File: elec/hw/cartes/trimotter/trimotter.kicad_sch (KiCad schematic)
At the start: 68 parts, among them J2 22053051, J3 2-1445055-2, J4 2-1445055-3, J5 3-794630-6, J6 3-794630-4, Q1 2N7002, U1 DRV8243HQDGQRQ1, U2 SN74LVC2T45DCU, U4 PCA9535PW

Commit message: trimotter schematic corrected after review. component placement done, routing tbd
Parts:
- removed R13: 10k 1%, cocotter_resistor:r0603_reflow, symbol cocotter_resistors:R_10k_0603_1%
- removed R14: 470R 1%, cocotter_resistor:r0603_reflow, symbol cocotter_resistors:R_470R_0603_1%
- added R13, R33, R34: 3k3 1%, cocotter_resistor:r0603_reflow, symbol cocotter_resistors:R_3k3_0603_1%
- added R14, R32: 1k 1%, cocotter_resistor:r0603_reflow, symbol cocotter_resistors:R_1k_0603_1%
- added R30, R31, R35: 0R, cocotter_resistor:r0603_reflow, symbol cocotter_resistors:R_0R_0603
- C3: value 1µF 50V -> 47µF 10V; footprint cocotter_capacitors:C_0805_2012Metric -> cocotter_capacitors:C_1206_3216Metric; symbol cocotter_capacitors:C_1µF_50V_0805 -> cocotter_capacitors:C_47µF_10V_1206_X5R; JLCPCB Part # C28323 -> C96123; Specification 1µF 50V X7R 0805 -> 47µF 10V X5R 1206
- D1, D3: value green, 0603 -> green, 1206; footprint cocotter_diodes:LED_0603_1608Metric -> cocotter_diodes:24-21-1206_reverse_mount; symbol cocotter_diodes:green_led_0603 -> cocotter_diodes:green_led_1206_reverse_mount; DIGIKEY_REF 3147-B19Y1UYG-20C000313U1930CT-ND -> (none); JLCPCB Part # C22371299 -> C2980185; MOUSER_REF 710-150060VS55040 -> (none)
- D2: value yellow, 0603 -> red, 1206; footprint cocotter_diodes:LED_0603_1608Metric -> cocotter_diodes:24-21-1206_reverse_mount; symbol cocotter_diodes:yellow_led_0603 -> cocotter_diodes:red_led_1206_reverse_mount; DIGIKEY_REF 150060YS55040 -> (none); JLCPCB Part # C965802 -> C2827254
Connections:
- net +3V3: now also R14.2, R32.2
- net VMOT: now also J4.2, R33.1
- net brake_3v3: now also U4.7 (IO0_3), R35.2; no longer J1.4 (brake_3v3), U4.5 (IO0_1)
- net ctc_left_3v3: now also U4.5 (IO0_1); no longer U4.7 (IO0_3)
- net ctc_right_3v3: now also U4.4 (IO0_0); no longer U4.6 (IO0_2)
- net encoder_A_5v: now also R30.2; no longer U2.6 (B2)
- net encoder_B_5v: now also R31.2; no longer U2.7 (B1)
- net nFAULT_3V3: now also U4.6 (IO0_2); no longer U4.4 (IO0_0)
- net vmot_absent_3v3: now also U4.20 (IO1_7); no longer U4.10 (IO0_6)
- net at TP5.1: now also U4.15 (IO1_2); no longer U4.16 (IO1_3)
- net at TP7.1: now also U4.17 (IO1_4); no longer U4.18 (IO1_5)
- net at D2.A: now also R14.1, R32.1
- net at D1.A: now also R13.2
- net at TP8.1: now also U4.18 (IO1_5); no longer U4.19 (IO1_6)
- net at TP9.1: now also U4.19 (IO1_6); no longer U4.20 (IO1_7)
- net at TP2.1: now also U4.10 (IO0_6); no longer U4.13 (IO1_0)
- net at TP3.1: now also U4.13 (IO1_0); no longer U4.14 (IO1_1)
- net at TP4.1: now also U4.14 (IO1_1); no longer U4.15 (IO1_2)
- net at TP6.1: now also U4.16 (IO1_3); no longer U4.17 (IO1_4)
- new net: J1.4 (brake_3v3), R35.1
- new net: R33.2, R34.1
- new net: R30.1, U2.6 (B2)
- new net: R31.1, U2.7 (B1)
- new net: R13.1, R34.2
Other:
- moved on the sheet: C3, D1, Q1, R27, R28, R29, TP2, TP3, TP4, TP5, TP6, TP7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

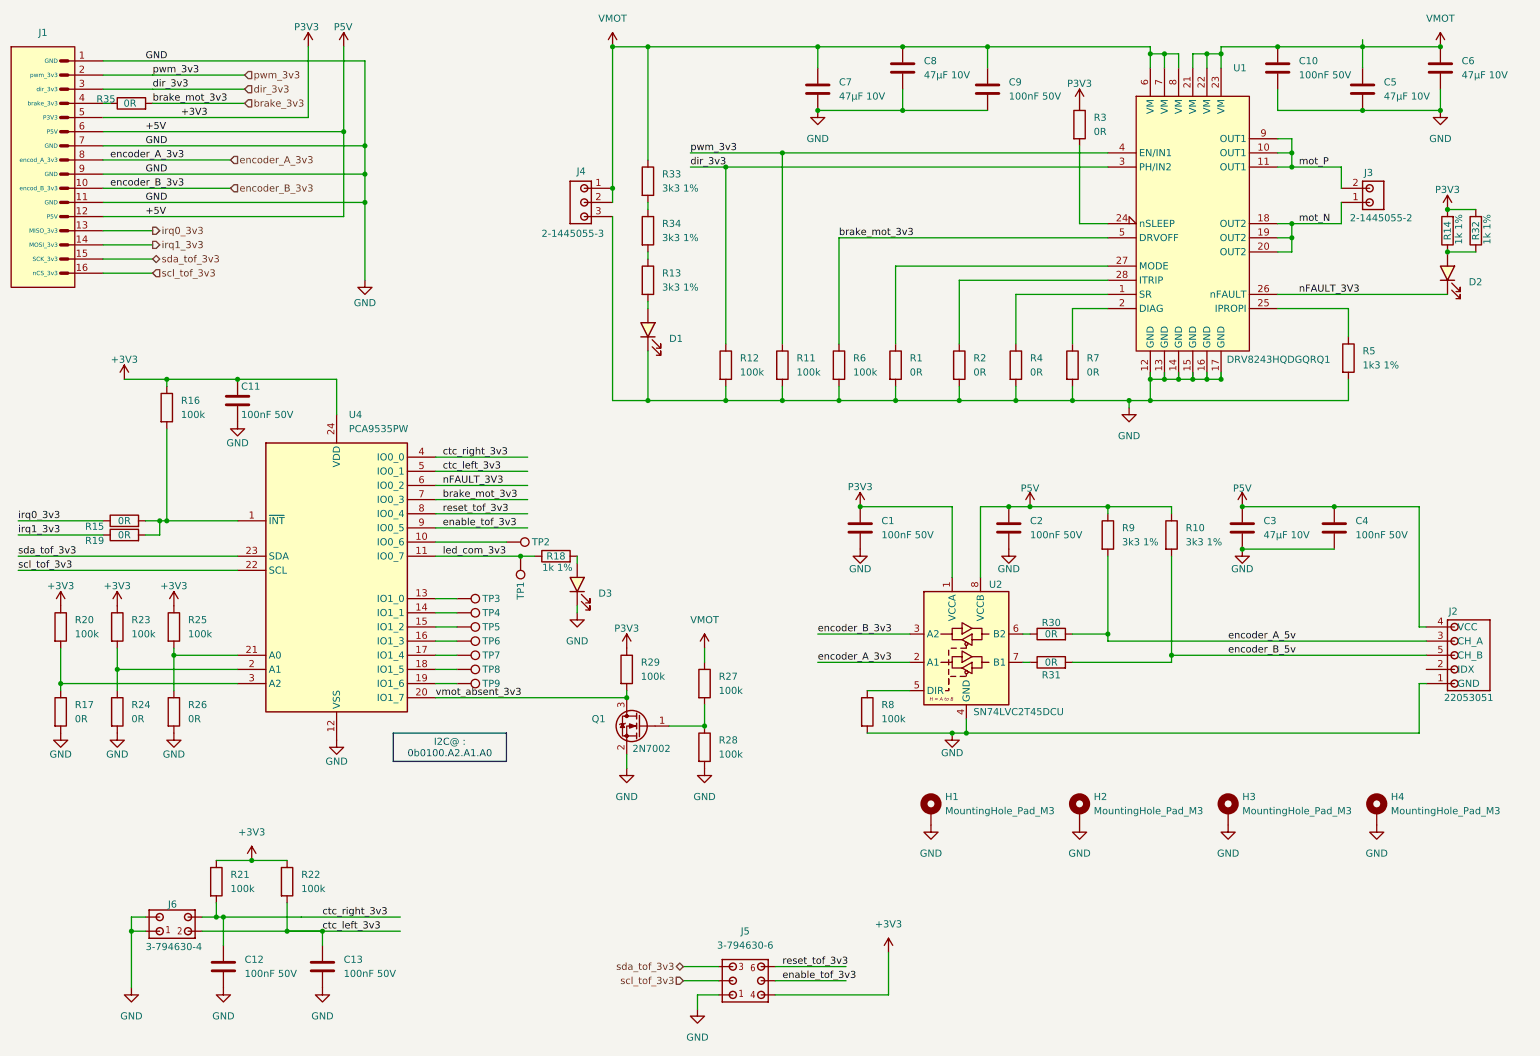
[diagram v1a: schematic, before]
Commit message: trimotter routing ready to review
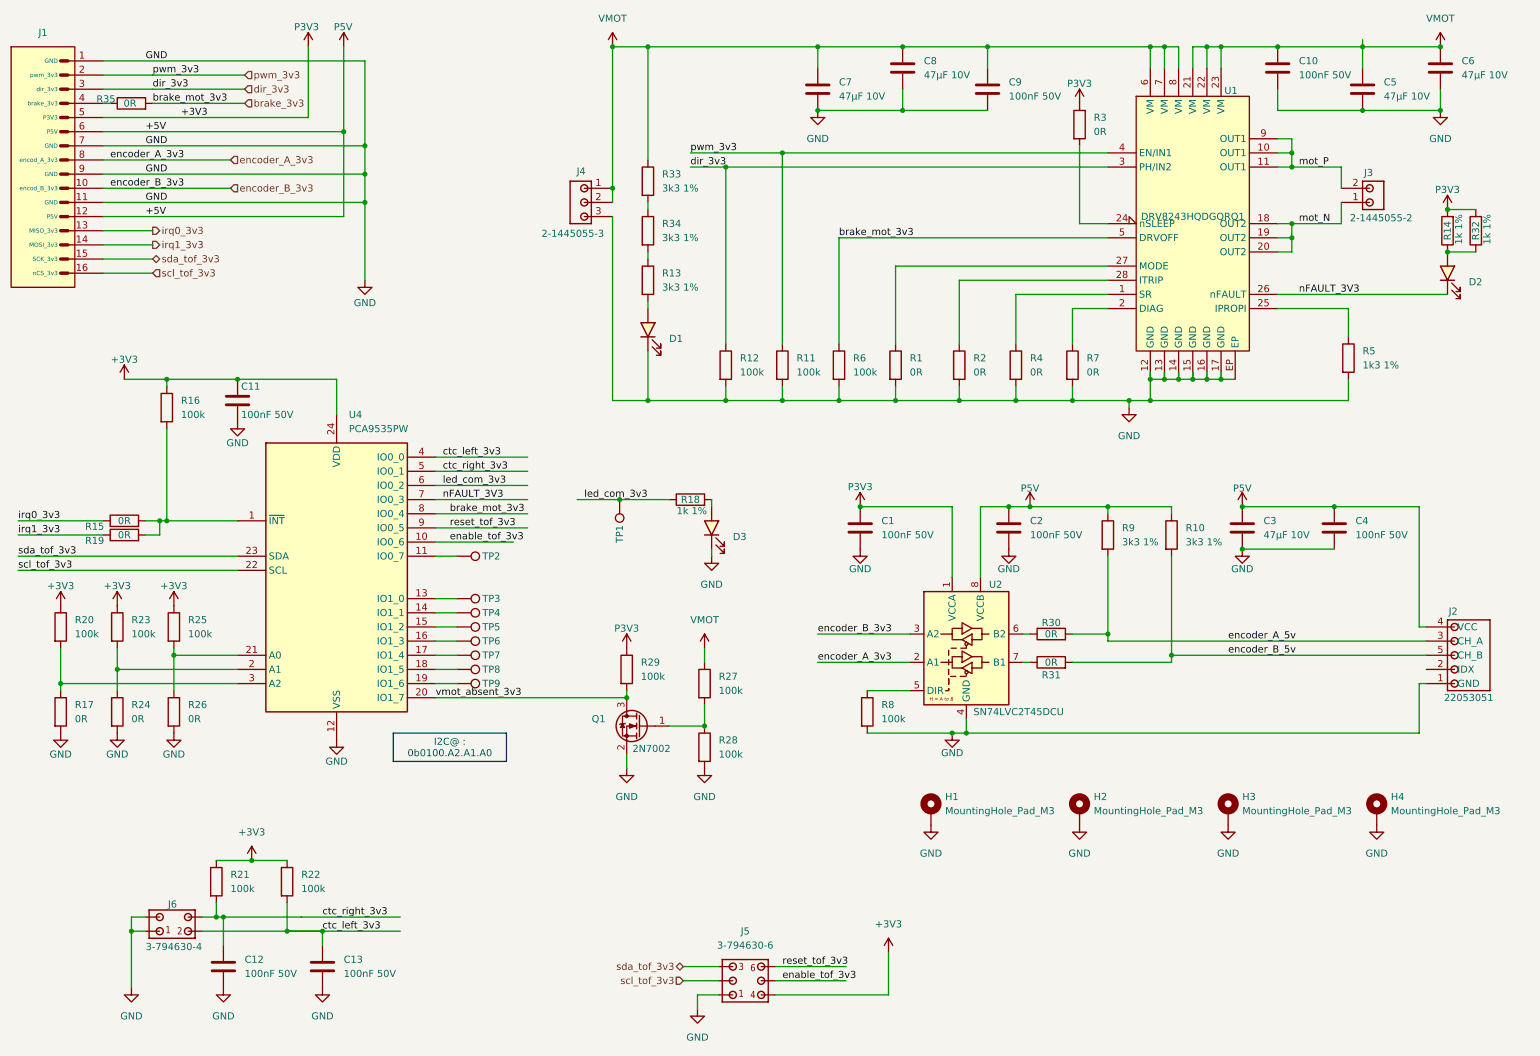
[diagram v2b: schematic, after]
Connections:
- net GND: now also U1.EP
- net brake_3v3: now also U4.8 (IO0_4); no longer U4.7 (IO0_3)
- net ctc_left_3v3: now also U4.4 (IO0_0); no longer U4.5 (IO0_1)
- net ctc_right_3v3: now also U4.5 (IO0_1); no longer U4.4 (IO0_0)
- net enable_tof_3v3: now also U4.10 (IO0_6); no longer U4.9 (IO0_5)
- net led_com_3v3: now also U4.6 (IO0_2); no longer U4.11 (IO0_7)
- net nFAULT_3V3: now also U4.7 (IO0_3); no longer U4.6 (IO0_2)
- net reset_tof_3v3: now also U4.9 (IO0_5); no longer U4.8 (IO0_4)
- net at TP2.1: now also U4.11 (IO0_7); no longer U4.10 (IO0_6)
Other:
- moved on the sheet: D3, R18

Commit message: jlcpcb part added
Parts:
- H1, H2, H3, H4: now in the parts list
- J1: JLCPCB Part # (none) -> C720217
- J2: JLCPCB Part # (none) -> C586992
- J3: JLCPCB Part # (none) -> C239446
- J4: JLCPCB Part # (none) -> C239447
- U1: JLCPCB Part # (none) -> C5250151
- U2: JLCPCB Part # (none) -> C15741
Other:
- moved on the sheet: R18, R5, TP1
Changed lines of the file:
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@@
 	)
 	(junction
-		(at 124.46 100.33)
-		(diameter 0)
-		(color 0 0 0 0)
-	)
-	(junction
 		(at 257.81 30.48)
 		(diameter 0)
@@
 	)
 	(junction
+		(at 124.46 97.79)
+		(diameter 0)
+		(color 0 0 0 0)
+	)
+	(junction
 		(at 44.45 128.27)
 		(diameter 0)
@@
 	(wire
 		(pts
-			(xy 116.84 100.33) (xy 124.46 100.33)
-		)
-		(stroke
-			(width 0)
-			(type default)
-		)
-	)
-	(wire
-		(pts
 			(xy 267.97 133.35) (xy 267.97 142.24)
 		)
@@
 	(wire
 		(pts
-			(xy 91.44 97.79) (xy 107.95 97.79)
+			(xy 91.44 97.79) (xy 124.46 97.79)
 		)
 		(stroke
@@
 	(wire
 		(pts
-			(xy 140.97 100.33) (xy 140.97 101.6)
+			(xy 140.97 97.79) (xy 140.97 101.6)
 		)
 		(stroke
@@
 	(wire
 		(pts
-			(xy 219.71 82.55) (xy 255.27 82.55)
+			(xy 219.71 82.55) (xy 256.54 82.55)
 		)
 		(stroke
@@
 	(wire
 		(pts
-			(xy 242.57 66.04) (xy 255.27 66.04)
+			(xy 242.57 66.04) (xy 256.54 66.04)
 		)
 		(stroke
@@
 	(wire
 		(pts
-			(xy 255.27 82.55) (xy 255.27 78.74)
+			(xy 256.54 82.55) (xy 256.54 78.74)
 		)
 		(stroke
@@
 	(wire
 		(pts
-			(xy 255.27 66.04) (xy 255.27 71.12)
+			(xy 256.54 66.04) (xy 256.54 71.12)
 		)
 		(stroke
@@
 	(wire
 		(pts
-			(xy 124.46 100.33) (xy 133.35 100.33)
+			(xy 124.46 97.79) (xy 133.35 97.79)
 		)
 		(stroke
@@
 		)
 	)
-	(label "led_com_3v3"
-		(at 118.11 100.33 0)
-		(effects
-			(font
-				(size 1.27 1.27)
-			)
-			(justify left bottom)
-		)
-	)
 	(label "mot_N"
 		(at 246.38 50.8 0)
@@
 		)
 		(property "Value" "DRV8243HQDGQRQ1"
-			(at 227.33 49.53 0)
+			(at 245.11 74.93 0)
 			(effects
 				(font
@@
 			)
 		)
+		(property "JLCPCB Part #" "C5250151"
+			(at 227.33 50.8 0)
+			(effects
+				(font
+					(size 1.27 1.27)
+				)
+				(hide yes)
+			)
+		)
 		(pin "12"
 		)
@@
 		(unit 1)
 		(exclude_from_sim yes)
-		(in_bom no)
+		(in_bom yes)
 		(on_board yes)
 		(dnp no)
@@
 		(dnp no)
 		(property "Reference" "J2"
-			(at 274.066 120.396 0)
+			(at 280.162 120.904 0)
 			(effects
 				(font
@@
 		)
 		(property "Value" "22053051"
-			(at 276.86 135.89 0)
+			(at 276.098 135.89 0)
 			(effects
 				(font
@@
 			)
 		)
+		(property "JLCPCB Part #" "C586992"
+			(at 269.24 128.27 0)
+			(effects
+				(font
+					(size 1.27 1.27)
+				)
+				(hide yes)
+			)
+		)
 		(pin "3"
 		)
@@
 		(unit 1)
 		(exclude_from_sim yes)
-		(in_bom no)
+		(in_bom yes)
 		(on_board yes)
 		(dnp no)
@@
 		(unit 1)
 		(exclude_from_sim yes)
-		(in_bom no)
+		(in_bom yes)
 		(on_board yes)
 		(dnp no)
@@
 		(dnp no)
 		(property "Reference" "J3"
-			(at 258.064 41.656 0)
+			(at 254 45.72 0)
 			(effects
 				(font
 					(size 1.27 1.27)
 				)
-				(justify right)
 			)
 		)
 		(property "Value" "2-1445055-2"
-			(at 255.524 49.784 0)
+			(at 258.572 49.276 0)
 			(effects
 				(font
 					(size 1.27 1.27)
 				)
-				(justify right)
 			)
 		)
@@
 			)
 		)
+		(property "JLCPCB Part #" "C239446"
+			(at 254 45.72 0)
+			(effects
+				(font
+					(size 1.27 1.27)
+				)
+				(hide yes)
+			)
+		)
 		(pin "2"
 		)
@@
 		(dnp no)
 		(property "Reference" "U2"
-			(at 190.754 115.57 0)
+			(at 180.34 116.078 0)
 			(effects
 				(font
 					(size 1.27 1.27)
 				)
-				(justify left)
 			)
 		)
 		(property "Value" "SN74LVC2T45DCU"
-			(at 187.96 138.43 0)
+			(at 188.214 138.43 0)
 			(effects
 				(font
@@
 			)
 		)
-		(property "JLCPCB Part #" ""
+		(property "JLCPCB Part #" "C15741"
 			(at 186.69 129.54 0)
 			(effects
@@
 	(symbol
 		(lib_id "cocotter_resistors:R_1k_0603_1%")
-		(at 137.16 100.33 90)
+		(at 137.16 97.79 90)
 		(unit 1)
 		(exclude_from_sim no)
@@
 		(dnp no)
 		(property "Reference" "R18"
-			(at 137.16 100.33 90)
+			(at 137.16 97.79 90)
 			(effects
 				(font
@@
 		)
 		(property "Value" "1k 1%"
-			(at 137.414 102.362 90)
+			(at 137.414 99.822 90)
 			(effects
 				(font
@@
 		)
 		(property "Footprint" "cocotter_resistor:r0603_reflow"
-			(at 137.16 102.108 90)
+			(at 137.16 99.568 90)
 			(effects
 				(font
@@
 		)
 		(property "Datasheet" "~"
-			(at 137.16 100.33 0)
+			(at 137.16 97.79 0)
 			(effects
 				(font
@@
 		)
 		(property "Description" "Resistor"
-			(at 137.16 100.33 0)
+			(at 137.16 97.79 0)
 			(effects
 				(font
@@
 		)
 		(property "Specification" "10k 0603 1% 100mW"
-			(at 137.16 100.33 0)
+			(at 137.16 97.79 0)
 			(effects
 				(font
@@
 		)
 		(property "mouser" "603-RC0603FR-10100KL"
-			(at 137.16 100.33 0)
+			(at 137.16 97.79 0)
 			(effects
 				(font
@@
 		)
 		(property "JLCPCB Part #" "C2991540"
-			(at 137.16 100.33 0)
+			(at 137.16 97.79 0)
 			(effects
 				(font
@@
 	(symbol
 		(lib_id "cocotter_others:TestPoint_for_pogo_pin-1mm")
-		(at 124.46 100.33 180)
+		(at 124.46 97.79 180)
 		(unit 1)
 		(exclude_from_sim no)
@@
 		(dnp no)
 		(property "Reference" "TP1"
-			(at 124.46 104.902 90)
+			(at 124.46 102.362 90)
 			(effects
 				(font
@@
 		)
 		(property "Value" "TestPoint"
-			(at 123.1901 105.41 90)
+			(at 123.1901 102.87 90)
 			(effects
 				(font
@@
 		)
 		(property "Footprint" "cocotter_others:testpoint-THT-0.5mm"
-			(at 119.38 100.33 0)
+			(at 119.38 97.79 0)
 			(effects
 				(font
@@
 		)
 		(property "Datasheet" "~"
-			(at 119.38 100.33 0)
+			(at 119.38 97.79 0)
 			(effects
 				(font
@@
 		)
 		(property "Description" "test point"
-			(at 124.46 100.33 0)
+			(at 124.46 97.79 0)
 			(effects
 				(font
@@
 	(symbol
 		(lib_id "cocotter_resistors:R_1k3_0603_1%")
-		(at 255.27 74.93 0)
+		(at 256.54 74.93 0)
 		(unit 1)
 		(exclude_from_sim no)
@@
 		(fields_autoplaced yes)
 		(property "Reference" "R5"
-			(at 257.81 73.6599 0)
+			(at 259.08 73.6599 0)
 			(effects
 				(font
@@
 		)
 		(property "Value" "1k3 1%"
-			(at 257.81 76.1999 0)
+			(at 259.08 76.1999 0)
 			(effects
 				(font
@@
 		)
 		(property "Footprint" "cocotter_resistor:r0603_reflow"
-			(at 253.492 74.93 90)
+			(at 254.762 74.93 90)
 			(effects
 				(font
@@
 		)
 		(property "Datasheet" "~"
-			(at 255.27 74.93 0)
+			(at 256.54 74.93 0)
 			(effects
 				(font
@@
 		)
 		(property "Description" "Resistor"
-			(at 255.27 74.93 0)
+			(at 256.54 74.93 0)
 			(effects
 				(font
@@
 		)
 		(property "Specification" "1k3 0603 1% 100mW"
-			(at 255.27 74.93 0)
+			(at 256.54 74.93 0)
 			(effects
 				(font
@@
 		)
 		(property "mouser" ""
-			(at 255.27 74.93 0)
+			(at 256.54 74.93 0)
 			(effects
 				(font
@@
 		)
 		(property "JLCPCB Part #" "C22767"
-			(at 255.27 74.93 0)
+			(at 256.54 74.93 0)
 			(effects
 				(font
@@
 		(unit 1)
 		(exclude_from_sim yes)
-		(in_bom no)
+		(in_bom yes)
 		(on_board yes)
 		(dnp no)
@@
 			)
 		)
+		(property "JLCPCB Part #" "C720217"
+			(at 29.21 40.64 0)
+			(effects
+				(font
+					(size 1.27 1.27)
+				)
+				(hide yes)
+			)
+		)
 		(pin "12"
 		)
@@
 		(dnp no)
 		(property "Reference" "J4"
-			(at 118.364 41.402 0)
+			(at 117.094 51.816 0)
 			(effects
 				(font
 					(size 1.27 1.27)
 				)
-				(justify right)
 			)
 		)
 		(property "Value" "2-1445055-3"
-			(at 121.666 52.578 0)
+			(at 117.602 41.91 0)
 			(effects
 				(font
 					(size 1.27 1.27)
 				)
-				(justify right)
 			)
 		)
@@
 			(effects
 				(font
+					(size 1.27 1.27)
+				)
+				(hide yes)
+			)
+		)
+		(property "JLCPCB Part #" "C239447"
+			(at 119.38 48.26 0)
+			(effects
+				(font
